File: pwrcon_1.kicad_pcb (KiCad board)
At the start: 2 copper layers, 85.1 x 48 mm, 53 parts, among them J1 CON3, J4 CON3, J5 Conn_01x03_Female, J6 Conn_01x04, J7 CON3, J8 Conn_01x03_Female, Q1 Q_PNP_BEC, U1 LM358, U2 ISOW7841DWE, U3 THVD1500D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

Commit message: Added missing 5VDC connection to isolator (isow7841dwe) and created new net vcc between isolator and esd/transceiver(thvd1500d). Changed layout.
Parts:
- removed TP5: TestPoint, TestPoint:TestPoint_Loop_D1.80mm_Drill1.0mm_Beaded
- moved C10 11.0 mm to (162.3, 87.4)
- moved C11 11.0 mm to (156.7, 87.7)
- moved U7 11.0 mm to (159.6, 87.9)
- moved R8 10.4 mm to (156.4, 82.1), turned to 90 degrees
- moved D5 7.55 mm to (152.7, 81.3), turned to 90 degrees
- moved D2 4.13 mm to (152.7, 89.7)
- moved U6 1.06 mm to (162.9, 70.7)
- moved U2 0.70 mm to (167.8, 80.3)
- moved C4 0.39 mm to (167.0, 63.9)
- moved C5 0.39 mm to (164.8, 63.9)
- moved D4 0.38 mm to (171.6, 88.0)
- moved D1 0.38 mm to (161.7, 94.0)
- moved R5 0.32 mm to (166.9, 103.1)
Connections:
- net Net-(C4-Pad2) renamed /vcc
- C7 pad 1: Net-(C7-Pad1) -> /5VDC
- C8 pad 1: Net-(C7-Pad1) -> /5VDC
- D5 pad 1: Net-(C7-Pad1) -> /5VDC
- U2 pad 1: Net-(C7-Pad1) -> /5VDC
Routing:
- net /5VDC: track 53.2 -> 38.8 mm
- net Net-(C7-Pad1): track 13.1 -> 0.00 mm
- net /vcc: track 38.8 -> 26.3 mm, vias 3 -> 5
- net GNDA: track 30.4 -> 41.3 mm, vias 4 -> 8
- net GND: track 195.9 -> 206.0 mm, vias 9 -> 10
- net /3V3: track 53.4 -> 48.9 mm
- net Net-(U2-Pad12): track 19.1 -> 16.4 mm
- net Net-(R4-Pad2): track 11.9 -> 14.5 mm, vias 0 -> 2
- net Net-(U2-Pad6): track 11.9 -> 13.0 mm
- net Net-(U2-Pad14): track 10.2 -> 9.22 mm
- net Net-(U2-Pad13): track 9.01 -> 9.72 mm
- net /RS485_RXD: track 8.04 -> 7.34 mm
- added copper zone on B.Cu, net /vcc
- added copper zone on F.Cu, net /vcc
- added copper zone on F.Cu, net GNDA

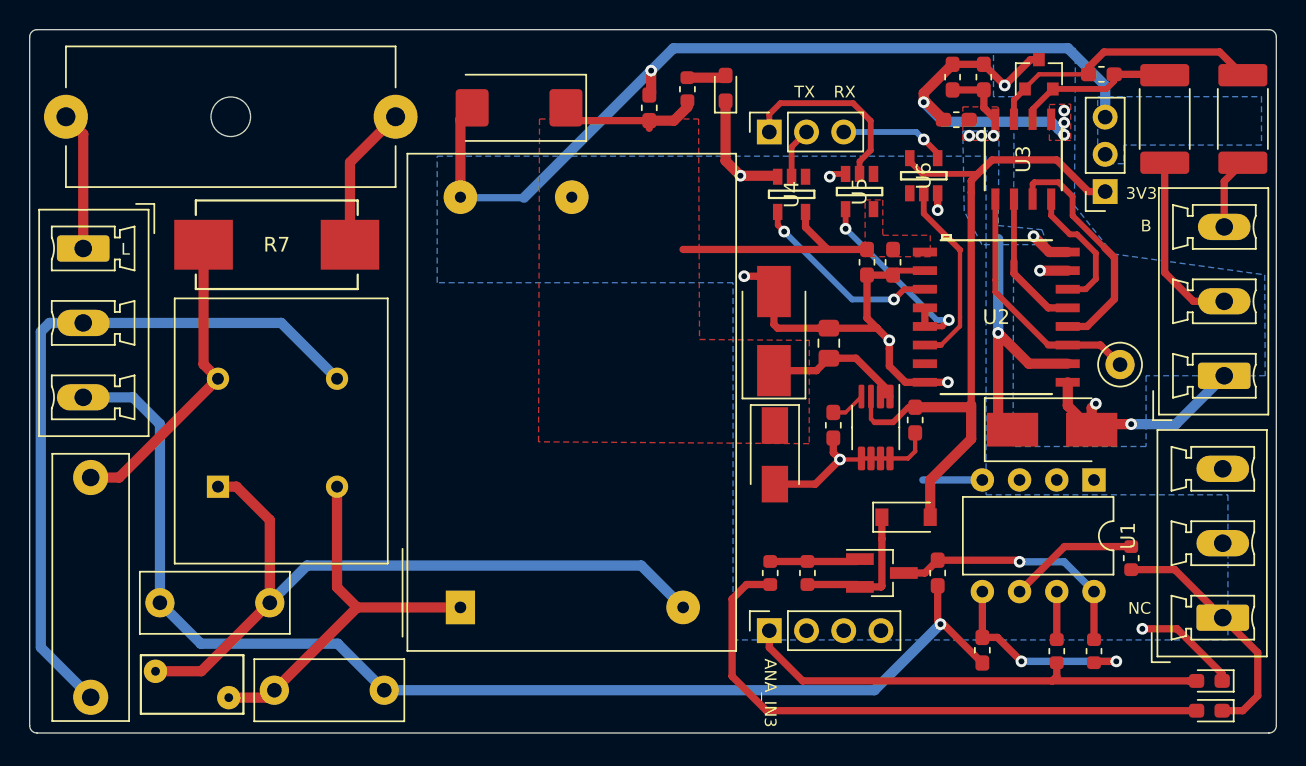
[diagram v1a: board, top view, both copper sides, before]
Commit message: Headers should now match cc3220modasf commit d3c2dc17dd42c882b5c02795b58cb5e5026f240b
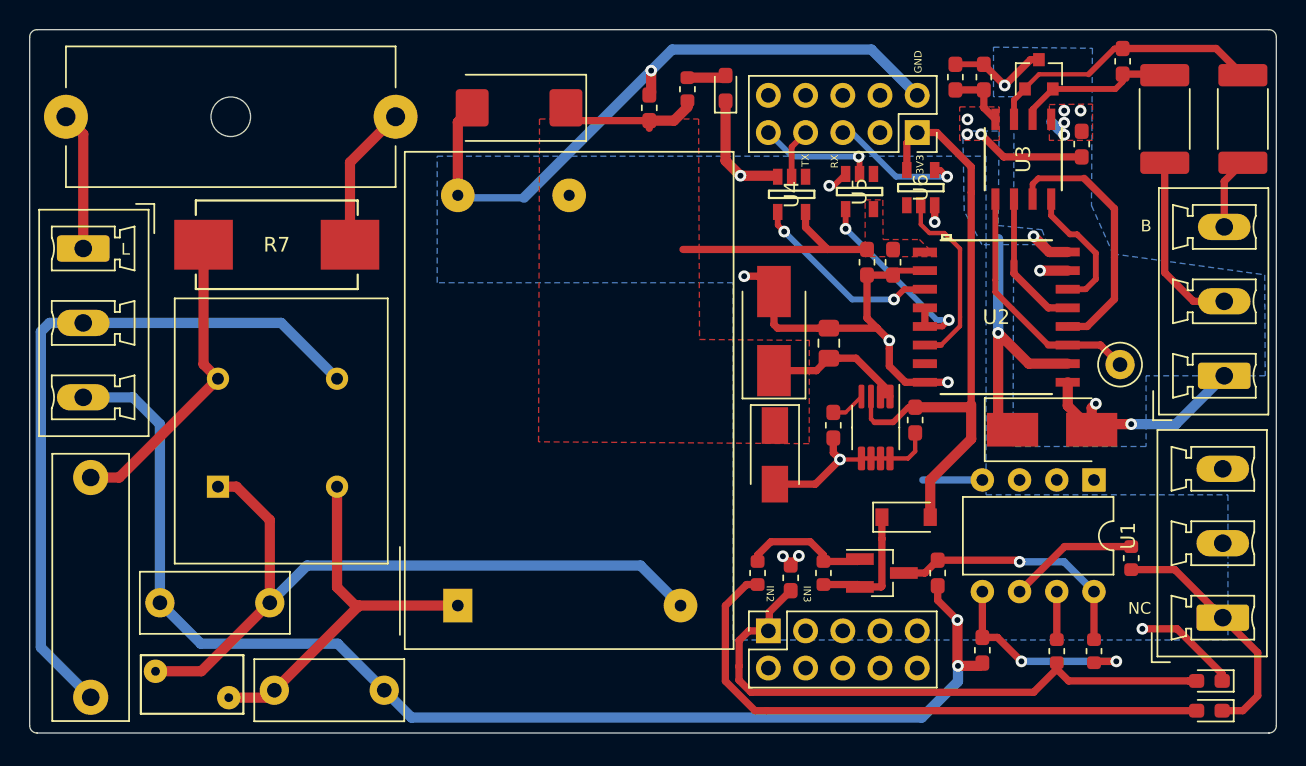
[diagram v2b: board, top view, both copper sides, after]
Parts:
- removed J5, J8: Conn_01x03_Female, Connector_PinSocket_2.54mm:PinSocket_1x03_P2.54mm_Vertical
- added C12: 0.1u, Capacitor_SMD:C_0603_1608Metric_Pad1.05x0.95mm_HandSolder, F.Cu at (153.8, 98.1)
- added J88: Conn_02x05_Odd_Even, Connector_PinSocket_2.54mm:PinSocket_2x05_P2.54mm_Vertical, F.Cu at (162.4, 67.7)
- J6: value Conn_01x04 -> Conn_02x05_Odd_Even; footprint Connector_PinSocket_2.54mm:PinSocket_1x04_P2.54mm_Vertical -> Connector_PinSocket_2.54mm:PinSocket_2x05_P2.54mm_Vertical
- moved C6 8.72 mm to (173.7, 68.5), turned to 90 degrees
- moved R12 1.70 mm to (176.5, 62.9), turned to 90 degrees
- moved R1 1.09 mm to (156.0, 97.8)
- moved R2 0.86 mm to (151.5, 97.8)
- moved U6 0.84 mm to (162.7, 71.5)
- moved PS1 0.22 mm to (131.1, 100.0)
- moved C5 0.19 mm to (165.0, 63.9)
- moved J6 0.06 mm to (152.3, 101.7)
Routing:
- net GNDA: track 41.3 -> 26.6 mm
- net Net-(C12-Pad1): track 33.0 -> 41.7 mm
- net GND: track 206.0 -> 197.6 mm, vias 10 -> 13
- net /vcc: track 26.3 -> 33.7 mm
- net /3V3: track 48.9 -> 42.3 mm
- net /RS485_EN: track 12.9 -> 8.05 mm, vias 0 -> 1
- net /Q1B: track 6.19 -> 8.68 mm
- net /RS485_RXD: track 7.34 -> 9.41 mm
- net Net-(U2-Pad12): track 16.4 -> 17.8 mm
- net /Q1E: track 9.88 -> 8.79 mm
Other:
- board text added: "GND"
- board text added: "IN2"
- board text added: "IN3"
- board text removed: "ANA_IN3"

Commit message: State at time of 2021-11-25 Aisler order
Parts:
- removed D1: D, Diode_SMD:D_SOD-123
- added R13: 0, Resistor_SMD:R_0603_1608Metric, F.Cu at (162.0, 91.1)
- added TP1: TestPoint, TestPoint:TestPoint_THTPad_D1.5mm_Drill0.7mm, F.Cu at (176.3, 79.5)
- added TP3: TestPoint, TestPoint:TestPoint_THTPad_D1.5mm_Drill0.7mm, F.Cu at (176.3, 82.9)
- C10: value 1u -> 4u7
- TP2: renamed from TP4; footprint TestPoint:TestPoint_Loop_D1.80mm_Drill1.0mm_Beaded -> TestPoint:TestPoint_Pad_D1.5mm
- U1: value LM358 -> LM358M; footprint Package_DIP:DIP-8_W7.62mm -> Package_SO:SOIC-8-1EP_3.9x4.9mm_P1.27mm_EP2.29x3mm
- moved TP2 10.4 mm to (174.1, 73.4)
- moved U1 5.92 mm to (172.1, 96.8)
- moved C10 5.50 mm to (159.3, 92.0)
- moved C11 4.23 mm to (156.7, 91.9)
- moved R9 3.15 mm to (148.5, 67.4)
- moved R3 2.08 mm to (176.0, 98.6)
- moved DR2 2.00 mm to (147.4, 65.0), turned to 0 degrees
- moved R5 1.92 mm to (168.7, 102.4), turned to 180 degrees
- moved U7 0.56 mm to (159.1, 88.2), turned to 0 degrees
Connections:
- C10 pad 1: /3V3 -> Net-(C10-Pad1)
- J88 pad 10: (no net) -> GND
- J88 pad 3: (no net) -> /RS485_RXD
- J88 pad 5: /RS485_RXD -> /RS485_TXD
- J88 pad 7: /RS485_TXD -> /RS485_EN
- J88 pad 8: (no net) -> GND
- J88 pad 9: /RS485_EN -> /5VDC
- Q1 pad 2: /Q1E -> /3V3
- R1 pad 1: /Q1E -> /3V3
- TP2 pad 1: Net-(TP4-Pad1) -> Net-(TP2-Pad1)
- U2 pad 11: Net-(TP4-Pad1) -> Net-(TP3-Pad1)
- U2 pad 14: Net-(U2-Pad14) -> Net-(TP2-Pad1)
- U3 pad 1: Net-(TP4-Pad1) -> Net-(TP3-Pad1)
- U3 pad 4: Net-(U2-Pad14) -> Net-(TP2-Pad1)
- U7 pad 3: /3V3 -> Net-(C10-Pad1)
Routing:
- net Net-(TP4-Pad1): track 16.9 -> 0.00 mm
- net Net-(TP3-Pad1): track 0.00 -> 16.6 mm
- net Net-(TP2-Pad1): track 0.00 -> 10.4 mm
- net Net-(U2-Pad14): track 9.22 -> 0.00 mm
- net /Q1E: track 8.79 -> 0.00 mm
- net GNDA: track 26.6 -> 18.2 mm, vias 8 -> 7
- net Net-(C10-Pad1): track 0.00 -> 6.41 mm
- net /3V3: track 42.3 -> 46.5 mm
- net /5VDC: track 38.8 -> 42.9 mm
- net Net-(TP1-Pad1): track 17.8 -> 20.3 mm
- net /RS485_EN: track 8.05 -> 5.51 mm
- net /RS485_TXD: track 3.48 -> 5.94 mm
- net Net-(C9-Pad2): track 17.5 -> 19.4 mm, vias 1 -> 2
- net /RS485_RXD: track 9.41 -> 7.58 mm
- net Net-(R4-Pad2): track 14.5 -> 12.8 mm
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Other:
- board text added: "5V"
